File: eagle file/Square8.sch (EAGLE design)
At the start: 28 parts, among them J3 CR2032-172, U1 ATmega328mu, U2 CH340T, U3 CN3065, X1 16MHz, X2 12MHz

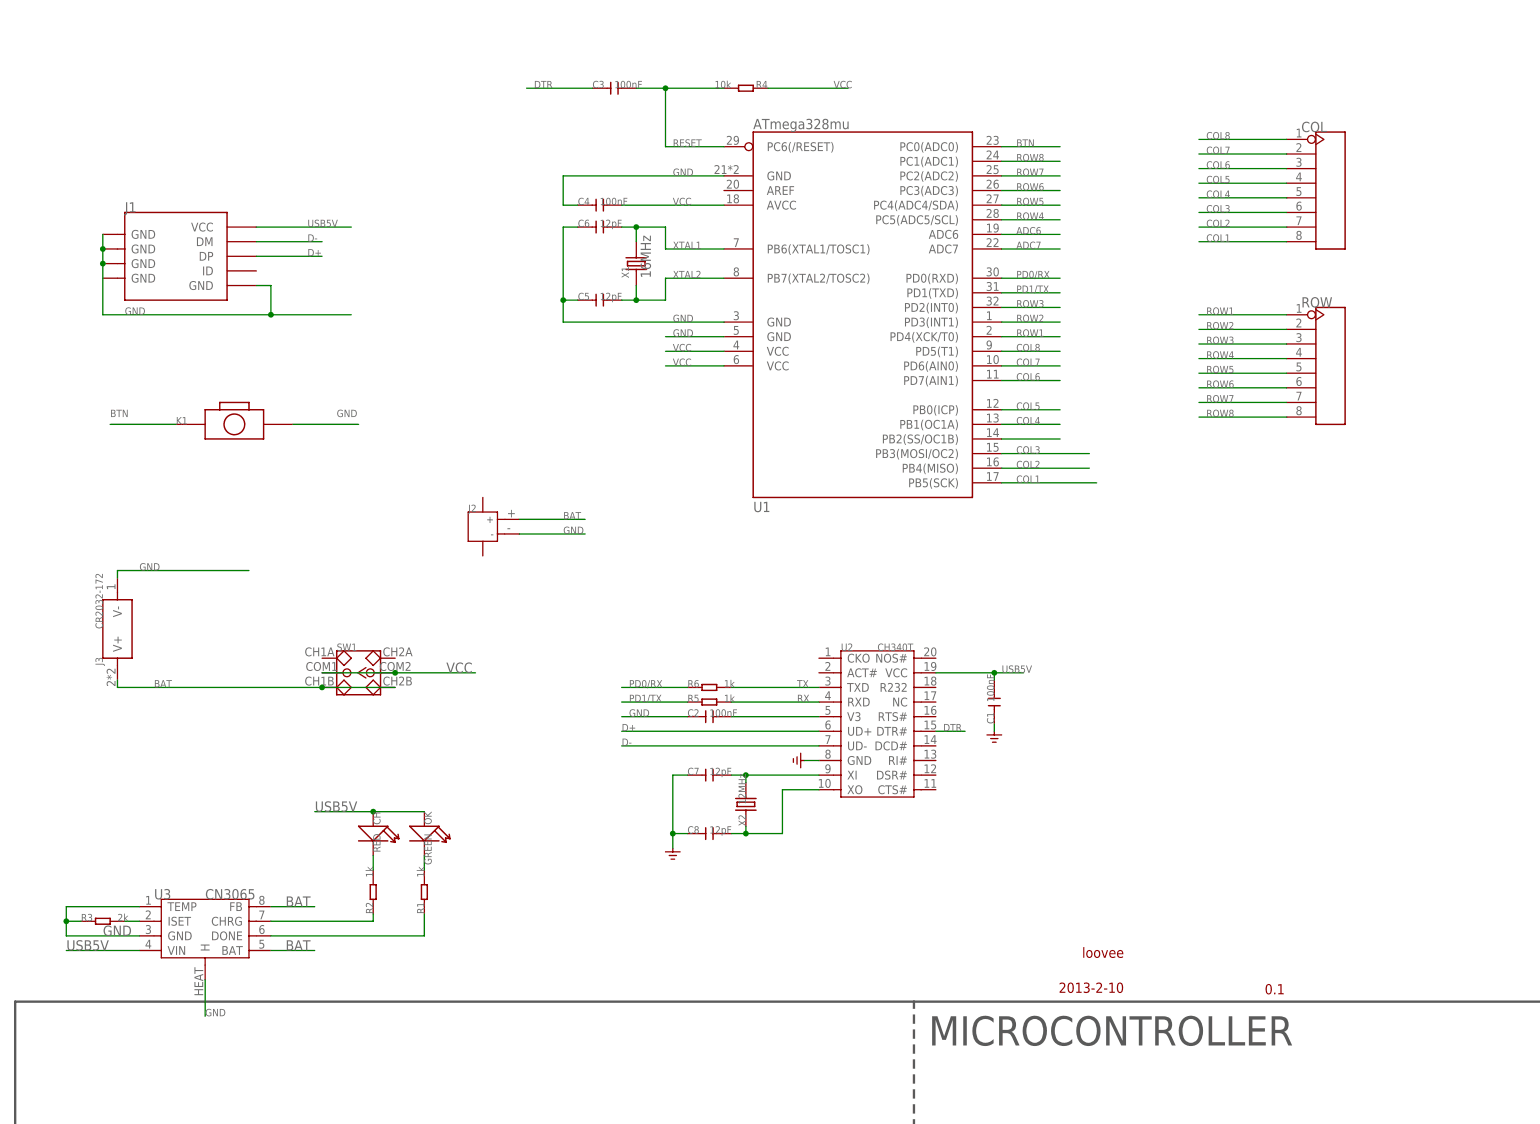
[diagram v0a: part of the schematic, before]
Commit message: add an two-dimension code to pcb
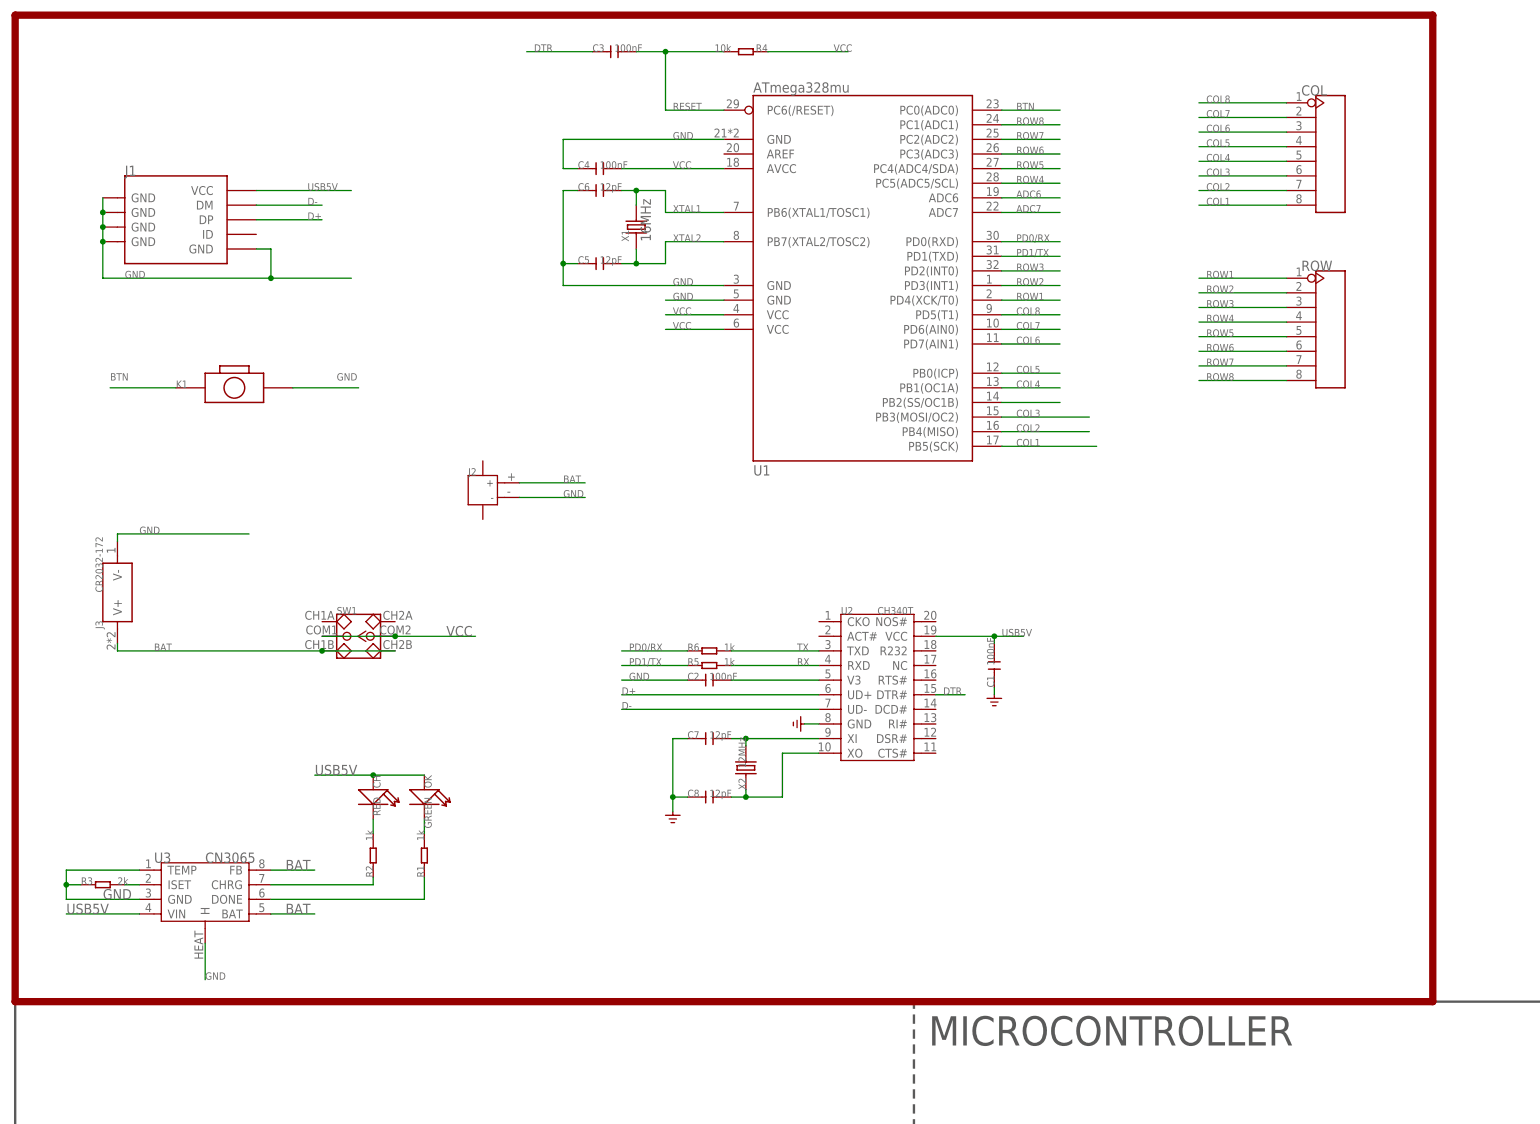
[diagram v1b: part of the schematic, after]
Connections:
- net GND: now also J1.GND@4
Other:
- note removed: "0.1"
- note removed: "2013-2-10"
- note removed: "loovee"
- moved on the sheet: C1, C2, C3, C4, C5, C6, C7, C8, CH, COL, J1, J2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

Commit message: update eagle file
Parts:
- removed J2: (no value), Connector :JACK-JST-2P-SMD-PW'2.0'
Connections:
- net COL6 renamed N$82
- net BAT: no longer J2.1
- net GND: no longer J2.2
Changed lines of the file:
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@@
 <part name="R5" library="Discrete" deviceset="R*" device="-0204/7" value="1k"/>
 <part name="C3" library="Discrete" deviceset="C*" device="'2.54'" value="100nF"/>
-<part name="J2" library="Connector " deviceset="JACK-JST-2P-SMD-PW" device="'2.0'"/>
 <part name="C2" library="Discrete" deviceset="C*" device="'2.54'" value="100nF"/>
 </parts>
@@
 <instance part="R5" gate="R" x="120.65" y="58.42"/>
 <instance part="C3" gate="C" x="104.14" y="165.1"/>
-<instance part="J2" gate="G$1" x="85.09" y="88.9"/>
 <instance part="C2" gate="C" x="120.65" y="55.88"/>
 </instances>
@@
 </segment>
 <segment>
-<pinref part="J2" gate="G$1" pin="2"/>
-<wire x1="99.06" y1="87.63" x2="87.63" y2="87.63" width="0.1524" layer="91"/>
-<label x="95.25" y="87.63" size="1.27" layer="95" ratio="10"/>
-</segment>
-<segment>
 <pinref part="C2" gate="C" pin="1"/>
 <wire x1="105.41" y1="55.88" x2="116.84" y2="55.88" width="0.1524" layer="91"/>
@@
 </segment>
 </net>
-<net name="COL6" class="0">
+<net name="N$82" class="0">
 <segment>
 <wire x1="181.61" y1="114.3" x2="171.45" y2="114.3" width="0.1524" layer="91"/>
@@
 </segment>
 <segment>
-<pinref part="J2" gate="G$1" pin="1"/>
-<wire x1="99.06" y1="90.17" x2="87.63" y2="90.17" width="0.1524" layer="91"/>
-<label x="95.25" y="90.17" size="1.27" layer="95" ratio="10"/>
-</segment>
-<segment>

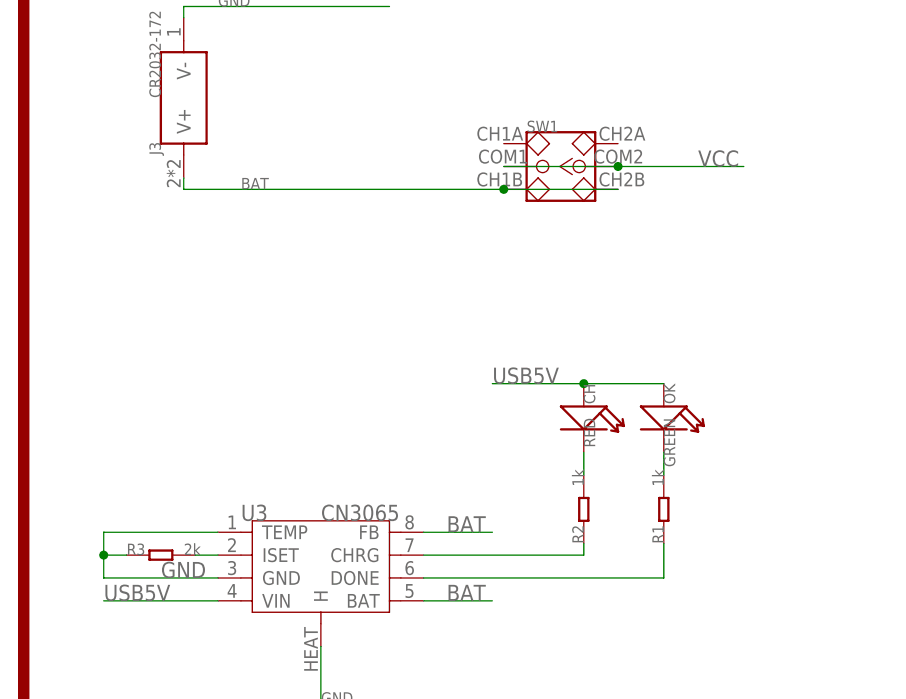
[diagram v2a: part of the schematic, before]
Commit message: add a pmos, when usb inserted, power will on
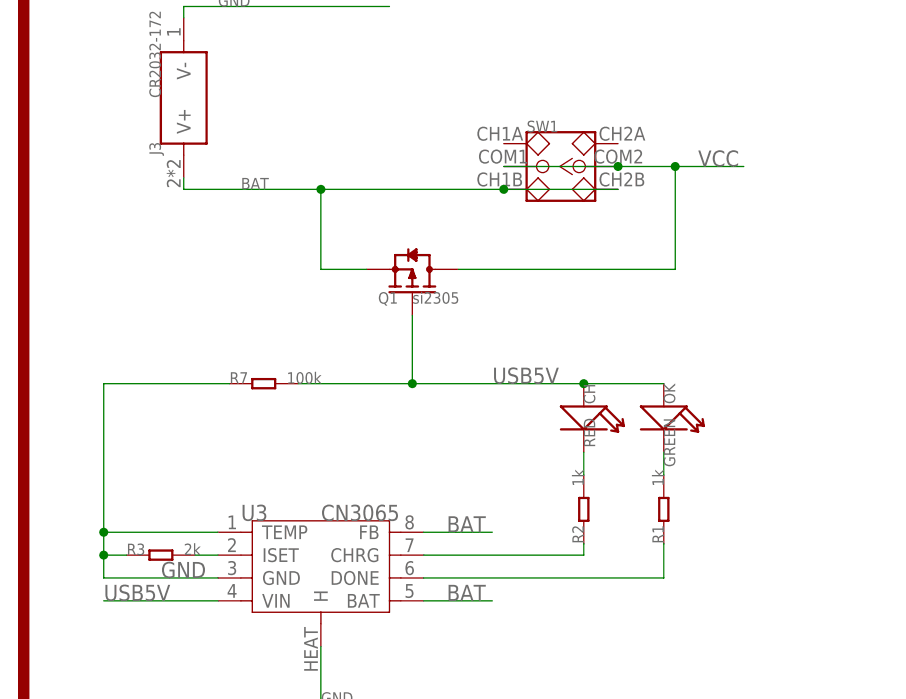
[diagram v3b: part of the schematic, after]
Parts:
- added Q1: si2305, Discrete:MOSFET-P'SI2323CDS/SI2305DS<BR>'
- added R7: 100k, Discrete:R-0603
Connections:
- net BAT: now also Q1.S
- net GND: now also R7.1
- net USB5V: now also Q1.G, R7.2
- net VCC: now also Q1.D
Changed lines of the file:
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@@
 <part name="C3" library="Discrete" deviceset="C*" device="'2.54'" value="100nF"/>
 <part name="C2" library="Discrete" deviceset="C*" device="'2.54'" value="100nF"/>
+<part name="Q1" library="Discrete" deviceset="MOSFET-P" device="'SI2323CDS/SI2305DS&lt;BR&gt;'" value="si2305"/>
+<part name="R7" library="Discrete" deviceset="R*" device="-0603" value="100k"/>
 </parts>
 <sheets>
@@
 <instance part="C3" gate="C" x="104.14" y="165.1"/>
 <instance part="C2" gate="C" x="120.65" y="55.88"/>
+<instance part="Q1" gate="MOS" x="43.18" y="52.07" rot="MR90"/>
+<instance part="R7" gate="R" x="26.67" y="39.37"/>
 </instances>
 <busses>
@@
 <pinref part="U3" gate="G$1" pin="TEMP"/>
 <pinref part="U3" gate="G$1" pin="GND"/>
+<pinref part="R7" gate="R" pin="1"/>
+<wire x1="22.86" y1="39.37" x2="8.89" y2="39.37" width="0.1524" layer="91"/>
+<wire x1="8.89" y1="39.37" x2="8.89" y2="22.86" width="0.1524" layer="91"/>
+<junction x="8.89" y="22.86"/>
 </segment>
 <segment>
@@
 <segment>
 <pinref part="SW1" gate="G$1" pin="COM2"/>
-<wire x1="66.04" y1="63.5" x2="80.01" y2="63.5" width="0.1524" layer="91"/>
+<wire x1="66.04" y1="63.5" x2="72.39" y2="63.5" width="0.1524" layer="91"/>
 <pinref part="SW1" gate="G$1" pin="COM1"/>
+<wire x1="72.39" y1="63.5" x2="80.01" y2="63.5" width="0.1524" layer="91"/>
 <wire x1="53.34" y1="63.5" x2="66.04" y2="63.5" width="0.1524" layer="91"/>
 <junction x="66.04" y="63.5"/>
 <label x="74.93" y="63.5" size="1.778" layer="95" ratio="10"/>
+<wire x1="72.39" y1="52.07" x2="72.39" y2="63.5" width="0.1524" layer="91"/>
+<junction x="72.39" y="63.5"/>
+<pinref part="Q1" gate="MOS" pin="D"/>
+<wire x1="72.39" y1="52.07" x2="48.26" y2="52.07" width="0.1524" layer="91"/>
 </segment>
 <segment>
@@
 <pinref part="CH" gate="LED" pin="+"/>
 <wire x1="71.12" y1="39.37" x2="62.23" y2="39.37" width="0.1524" layer="91"/>
-<wire x1="52.07" y1="39.37" x2="62.23" y2="39.37" width="0.1524" layer="91"/>
 <junction x="62.23" y="39.37"/>
 <label x="52.07" y="39.37" size="1.778" layer="95" ratio="10"/>
+<wire x1="62.23" y1="39.37" x2="43.18" y2="39.37" width="0.1524" layer="91"/>
+<pinref part="R7" gate="R" pin="2"/>
+<pinref part="Q1" gate="MOS" pin="G"/>
+<wire x1="43.18" y1="39.37" x2="30.48" y2="39.37" width="0.1524" layer="91"/>
+<wire x1="43.18" y1="46.99" x2="43.18" y2="39.37" width="0.1524" layer="91"/>
+<junction x="43.18" y="39.37"/>
 </segment>
 <segment>
@@
 <wire x1="17.78" y1="62.23" x2="17.78" y2="60.96" width="0.1524" layer="91"/>
 <label x="24.13" y="60.96" size="1.27" layer="95" ratio="10"/>
-<wire x1="53.34" y1="60.96" x2="17.78" y2="60.96" width="0.1524" layer="91"/>
+<wire x1="53.34" y1="60.96" x2="33.02" y2="60.96" width="0.1524" layer="91"/>
 <pinref part="SW1" gate="G$1" pin="CH1B"/>
 <pinref part="SW1" gate="G$1" pin="CH2B"/>
+<wire x1="33.02" y1="60.96" x2="17.78" y2="60.96" width="0.1524" layer="91"/>
 <wire x1="66.04" y1="60.96" x2="53.34" y2="60.96" width="0.1524" layer="91"/>
 <junction x="53.34" y="60.96"/>
-</segment>
-<segment>
+<junction x="33.02" y="60.96"/>
+<wire x1="33.02" y1="52.07" x2="33.02" y2="60.96" width="0.1524" layer="91"/>
+<pinref part="Q1" gate="MOS" pin="S"/>
+<wire x1="33.02" y1="52.07" x2="38.1" y2="52.07" width="0.1524" layer="91"/>
+</segment>
+<segment>

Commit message: improve pcb
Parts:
- added P1: (no value), Discrete:PAD-JUMPER-2P
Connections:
- new net N$86: P1.2, Q1.G, R7.2
- net USB5V: now also P1.1; no longer Q1.G, R7.2
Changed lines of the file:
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@@
 <part name="Q1" library="Discrete" deviceset="MOSFET-P" device="'SI2323CDS/SI2305DS&lt;BR&gt;'" value="si2305"/>
 <part name="R7" library="Discrete" deviceset="R*" device="-0603" value="100k"/>
+<part name="P1" library="Discrete" deviceset="PAD-JUMPER-2P" device=""/>
+<part name="U$2" library="Power or GND " deviceset="GND_POWER" device=""/>
+<part name="U$3" library="Power or GND " deviceset="GND_POWER" device=""/>
 </parts>
 <sheets>
@@
 <instance part="Q1" gate="MOS" x="43.18" y="52.07" rot="MR90"/>
 <instance part="R7" gate="R" x="26.67" y="39.37"/>
+<instance part="P1" gate="G$1" x="50.8" y="35.56" rot="R90"/>
+<instance part="U$2" gate="G$1" x="5.08" y="19.05"/>
+<instance part="U$3" gate="G$1" x="100.33" y="53.34"/>
 </instances>
 <busses>
@@
 <label x="21.59" y="81.28" size="1.27" layer="95" ratio="10"/>
 <wire x1="40.64" y1="81.28" x2="17.78" y2="81.28" width="0.1524" layer="91"/>
-</segment>
-<segment>
-<wire x1="8.89" y1="17.78" x2="8.89" y2="20.32" width="0.1524" layer="91"/>
-<wire x1="8.89" y1="20.32" x2="11.43" y2="20.32" width="0.1524" layer="91"/>
-<wire x1="8.89" y1="22.86" x2="8.89" y2="20.32" width="0.1524" layer="91"/>
-<wire x1="21.59" y1="22.86" x2="8.89" y2="22.86" width="0.1524" layer="91"/>
-<wire x1="21.59" y1="17.78" x2="8.89" y2="17.78" width="0.1524" layer="91"/>
-<junction x="8.89" y="20.32"/>
-<label x="15.24" y="17.78" size="1.778" layer="95"/>
-<pinref part="R3" gate="R" pin="1"/>
-<pinref part="U3" gate="G$1" pin="TEMP"/>
-<pinref part="U3" gate="G$1" pin="GND"/>
-<pinref part="R7" gate="R" pin="1"/>
-<wire x1="22.86" y1="39.37" x2="8.89" y2="39.37" width="0.1524" layer="91"/>
-<wire x1="8.89" y1="39.37" x2="8.89" y2="22.86" width="0.1524" layer="91"/>
-<junction x="8.89" y="22.86"/>
 </segment>
 <segment>
@@
 </segment>
 <segment>
+<pinref part="U$2" gate="G$1" pin="GND"/>
+<wire x1="5.08" y1="19.05" x2="5.08" y2="20.32" width="0.1524" layer="91"/>
+<wire x1="8.89" y1="17.78" x2="8.89" y2="20.32" width="0.1524" layer="91"/>
+<wire x1="8.89" y1="20.32" x2="11.43" y2="20.32" width="0.1524" layer="91"/>
+<wire x1="8.89" y1="22.86" x2="8.89" y2="20.32" width="0.1524" layer="91"/>
+<wire x1="21.59" y1="22.86" x2="8.89" y2="22.86" width="0.1524" layer="91"/>
+<wire x1="21.59" y1="17.78" x2="8.89" y2="17.78" width="0.1524" layer="91"/>
+<junction x="8.89" y="20.32"/>
+<label x="15.24" y="17.78" size="1.778" layer="95"/>
+<pinref part="R3" gate="R" pin="1"/>
+<pinref part="U3" gate="G$1" pin="TEMP"/>
+<pinref part="U3" gate="G$1" pin="GND"/>
+<pinref part="R7" gate="R" pin="1"/>
+<wire x1="22.86" y1="39.37" x2="8.89" y2="39.37" width="0.1524" layer="91"/>
+<wire x1="8.89" y1="39.37" x2="8.89" y2="22.86" width="0.1524" layer="91"/>
+<junction x="8.89" y="22.86"/>
+<wire x1="5.08" y1="20.32" x2="8.89" y2="20.32" width="0.1524" layer="91"/>
+</segment>
+<segment>
+<pinref part="U$3" gate="G$1" pin="GND"/>
+<wire x1="100.33" y1="53.34" x2="100.33" y2="55.88" width="0.1524" layer="91"/>
 <pinref part="C2" gate="C" pin="1"/>
-<wire x1="105.41" y1="55.88" x2="116.84" y2="55.88" width="0.1524" layer="91"/>
+<wire x1="100.33" y1="55.88" x2="116.84" y2="55.88" width="0.1524" layer="91"/>
 <label x="106.68" y="55.88" size="1.27" layer="95" ratio="10"/>
 </segment>
@@
 <segment>
 <pinref part="J1" gate="USB" pin="VCC"/>
-<wire x1="41.91" y1="140.97" x2="58.42" y2="140.97" width="0.1524" layer="91"/>
-<label x="50.8" y="140.97" size="1.27" layer="95" ratio="10"/>
+<wire x1="41.91" y1="140.97" x2="53.34" y2="140.97" width="0.1524" layer="91"/>
+<label x="46.99" y="140.97" size="1.27" layer="95" ratio="10"/>
 </segment>
 <segment>
@@
 <label x="8.89" y="15.24" size="1.778" layer="95"/>
 <pinref part="U3" gate="G$1" pin="VIN"/>
-</segment>
-<segment>
-<pinref part="OK" gate="LED" pin="+"/>
-<pinref part="CH" gate="LED" pin="+"/>
-<wire x1="71.12" y1="39.37" x2="62.23" y2="39.37" width="0.1524" layer="91"/>
-<junction x="62.23" y="39.37"/>
-<label x="52.07" y="39.37" size="1.778" layer="95" ratio="10"/>
-<wire x1="62.23" y1="39.37" x2="43.18" y2="39.37" width="0.1524" layer="91"/>
-<pinref part="R7" gate="R" pin="2"/>
-<pinref part="Q1" gate="MOS" pin="G"/>
-<wire x1="43.18" y1="39.37" x2="30.48" y2="39.37" width="0.1524" layer="91"/>
-<wire x1="43.18" y1="46.99" x2="43.18" y2="39.37" width="0.1524" layer="91"/>
-<junction x="43.18" y="39.37"/>
 </segment>
 <segment>
@@
 <wire x1="175.26" y1="63.5" x2="170.18" y2="63.5" width="0.1524" layer="91"/>
 <label x="171.45" y="63.5" size="1.27" layer="95" ratio="10"/>
+</segment>
+<segment>
+<pinref part="CH" gate="LED" pin="+"/>
+<pinref part="OK" gate="LED" pin="+"/>
+<wire x1="71.12" y1="39.37" x2="62.23" y2="39.37" width="0.1524" layer="91"/>
+<label x="62.23" y="40.64" size="1.778" layer="95" ratio="10"/>
+<pinref part="P1" gate="G$1" pin="1"/>
+<wire x1="62.23" y1="39.37" x2="52.07" y2="39.37" width="0.1524" layer="91"/>
+<wire x1="52.07" y1="39.37" x2="52.07" y2="38.1" width="0.1524" layer="91"/>
+<junction x="62.23" y="39.37"/>
 </segment>
 </net>
@@
 </segment>
 </net>
+<net name="N$86" class="0">
+<segment>
+<pinref part="P1" gate="G$1" pin="2"/>
+<wire x1="49.53" y1="38.1" x2="49.53" y2="39.37" width="0.1524" layer="91"/>
+<pinref part="R7" gate="R" pin="2"/>
+<wire x1="49.53" y1="39.37" x2="43.18" y2="39.37" width="0.1524" layer="91"/>
+<pinref part="Q1" gate="MOS" pin="G"/>
+<wire x1="43.18" y1="39.37" x2="30.48" y2="39.37" width="0.1524" layer="91"/>
+<wire x1="43.18" y1="46.99" x2="43.18" y2="39.37" width="0.1524" layer="91"/>
+<junction x="43.18" y="39.37"/>
+</segment>
+</net>
+<net name="N$87" class="0">
+<segment>
+<wire x1="49.53" y1="35.56" x2="52.07" y2="35.56" width="0.1524" layer="91"/>
+</segment>
+</net>
